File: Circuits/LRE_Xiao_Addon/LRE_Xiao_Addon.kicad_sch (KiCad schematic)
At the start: 13 parts, among them J1 Conn_01x06_Socket, J3 Conn_01x06_Socket, J4 Conn_01x02_Pin, Q1 S8050, Q2 S8050, Q3 S8050

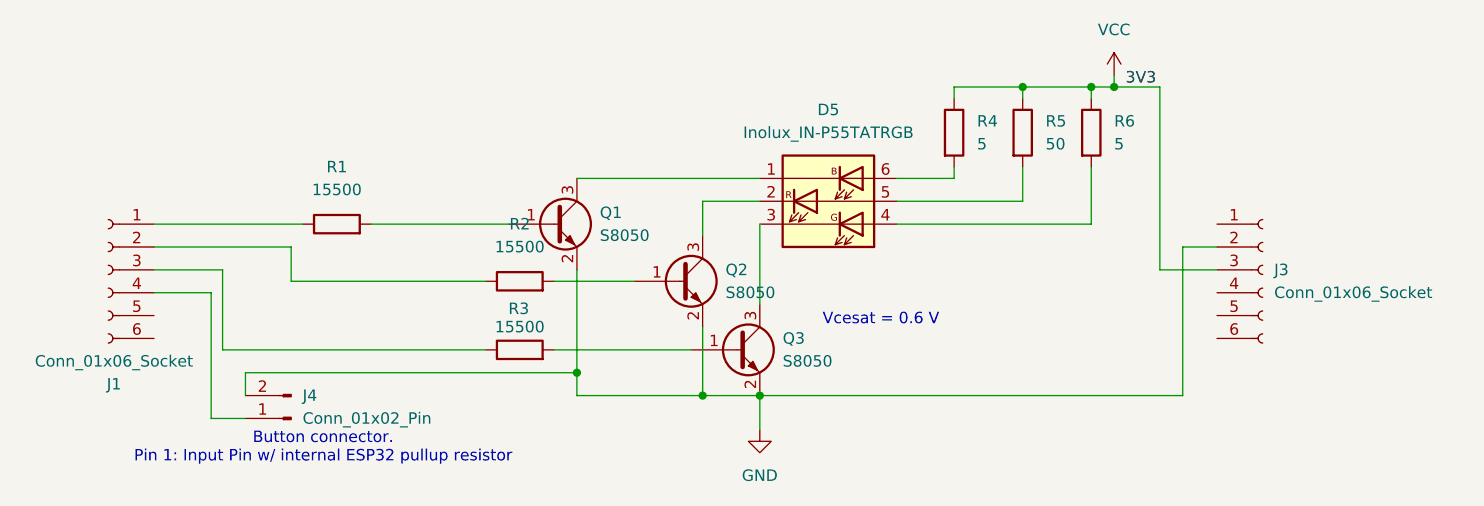
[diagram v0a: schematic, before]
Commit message: updated resistors
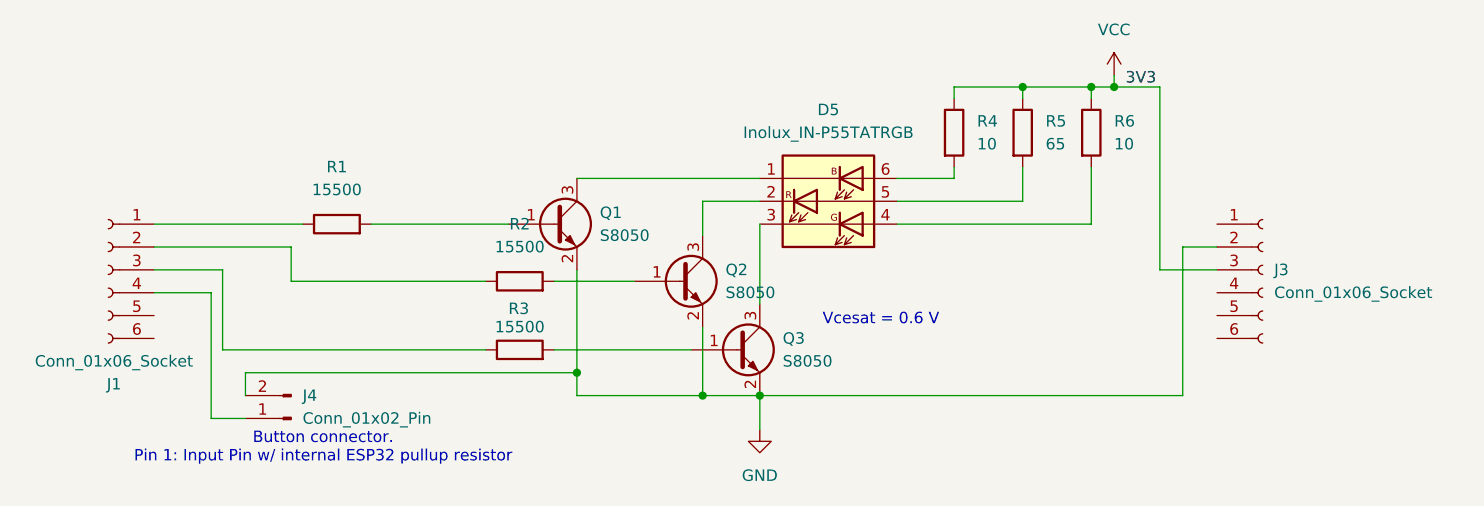
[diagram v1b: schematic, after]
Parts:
- R4, R6: value 5 -> 10
- R5: value 50 -> 65
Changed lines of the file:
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@@
 			)
 		)
-		(property "Value" "5"
+		(property "Value" "10"
 			(at 111.76 31.7499 0)
 			(effects
@@
 			)
 		)
-		(property "Value" "50"
+		(property "Value" "65"
 			(at 119.38 31.7499 0)
 			(effects
@@
 			)
 		)
-		(property "Value" "5"
+		(property "Value" "10"
 			(at 127 31.7499 0)
 			(effects

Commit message: USB Port accessible, updated color scheme
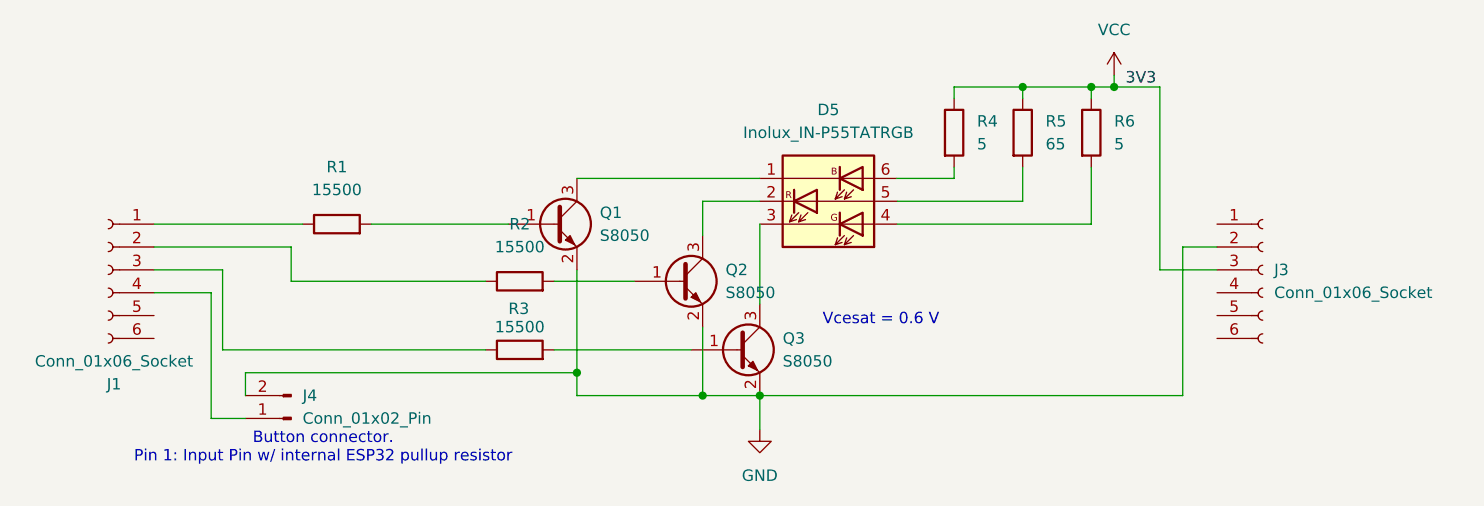
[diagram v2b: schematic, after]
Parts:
- R4, R6: value 10 -> 5
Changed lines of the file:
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@@
 			)
 		)
-		(property "Value" "10"
+		(property "Value" "5"
 			(at 111.76 31.7499 0)
 			(effects
@@
 			)
 		)
-		(property "Value" "10"
+		(property "Value" "5"
 			(at 127 31.7499 0)
 			(effects

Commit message: adjust resistors
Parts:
- R4, R6: value 5 -> 10,8
- R5: value 65 -> 60,8
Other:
- note added: "Vce = 0.084 V @ 20mA Ic (measured)"
- note removed: "Vcesat = 0.6 V"
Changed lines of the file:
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@@
 	(generator_version "9.0")
 	(paper "A4")
-	(text "Vcesat = 0.6 V"
-		(exclude_from_sim no)
-		(at 101.092 51.308 0)
+	(text "Vce = 0.084 V @ 20mA Ic (measured)"
+		(exclude_from_sim no)
+		(at 113.792 53.34 0)
 		(effects
 			(font
@@
 			)
 		)
-		(property "Datasheet" "https://mm.digikey.com/Volume0/opasdata/d220001/medias/docus/7158/5272_S8050.pdf"
+		(property "Datasheet" ""
 			(at 78.74 46.99 0)
 			(effects
@@
 		(dnp no)
 		(property "Reference" "R2"
-			(at 60.96 40.64 90)
+			(at 60.96 43.18 90)
 			(effects
 				(font
@@
 		)
 		(property "Value" "15500"
-			(at 60.96 43.18 90)
+			(at 60.96 44.958 90)
 			(effects
 				(font
@@
 		(on_board yes)
 		(dnp no)
-		(fields_autoplaced yes)
 		(property "Reference" "R4"
 			(at 111.76 29.2099 0)
@@
 			)
 		)
-		(property "Value" "5"
-			(at 111.76 31.7499 0)
+		(property "Value" "10,8"
+			(at 110.998 31.75 0)
 			(effects
 				(font
@@
 		(on_board yes)
 		(dnp no)
-		(fields_autoplaced yes)
 		(property "Reference" "R5"
 			(at 119.38 29.2099 0)
@@
 			)
 		)
-		(property "Value" "65"
-			(at 119.38 31.7499 0)
+		(property "Value" "60,8"
+			(at 118.364 31.75 0)
 			(effects
 				(font
@@
 			)
 		)
-		(property "Datasheet" "https://mm.digikey.com/Volume0/opasdata/d220001/medias/docus/7158/5272_S8050.pdf"
+		(property "Datasheet" ""
 			(at 85.09 54.61 0)
 			(effects
@@
 		(on_board yes)
 		(dnp no)
-		(fields_autoplaced yes)
 		(property "Reference" "R6"
 			(at 127 29.2099 0)
@@
 			)
 		)
-		(property "Value" "5"
-			(at 127 31.7499 0)
+		(property "Value" "10,8"
+			(at 127 31.75 0)
 			(effects
 				(font
@@
 		(on_board yes)
 		(dnp no)
-		(fields_autoplaced yes)
 		(property "Reference" "R1"
-			(at 40.64 34.29 90)
+			(at 40.64 36.83 90)
 			(do_not_autoplace yes)
 			(effects
@@
 		)
 		(property "Value" "15500"
-			(at 40.64 36.83 90)
+			(at 40.894 38.608 90)
 			(effects
 				(font
@@
 			)
 		)
-		(property "Datasheet" "https://mm.digikey.com/Volume0/opasdata/d220001/medias/docus/7158/5272_S8050.pdf"
+		(property "Datasheet" ""
 			(at 64.77 40.64 0)
 			(effects

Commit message: update hardware info
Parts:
- R4, R6: value 10,8 -> 11
- R5: value 60,8 -> 61
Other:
- note added: "Vce = 0.084 V @ 20mA Ic (measured) assuming Vce = 0,08V @ 20 mA for calculation"
- note removed: "Vce = 0.084 V @ 20mA Ic (measured)"
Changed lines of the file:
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@@
 	(generator_version "9.0")
 	(paper "A4")
-	(text "Vce = 0.084 V @ 20mA Ic (measured)"
-		(exclude_from_sim no)
-		(at 113.792 53.34 0)
+	(text "Vce = 0.084 V @ 20mA Ic (measured)\nassuming Vce = 0,08V @ 20 mA for calculation"
+		(exclude_from_sim no)
+		(at 113.538 49.53 0)
 		(effects
 			(font
@@
 			)
 		)
-		(property "Datasheet" ""
+		(property "Datasheet" "https://mm.digikey.com/Volume0/opasdata/d220001/medias/docus/7158/5272_S8050.pdf"
 			(at 78.74 46.99 0)
 			(effects
@@
 			)
 		)
-		(property "Value" "10,8"
+		(property "Value" "11"
 			(at 110.998 31.75 0)
 			(effects
@@
 			)
 		)
-		(property "Value" "60,8"
+		(property "Value" "61"
 			(at 118.364 31.75 0)
 			(effects
@@
 			)
 		)
-		(property "Datasheet" ""
+		(property "Datasheet" "https://mm.digikey.com/Volume0/opasdata/d220001/medias/docus/7158/5272_S8050.pdf"
 			(at 85.09 54.61 0)
 			(effects
@@
 			)
 		)
-		(property "Value" "10,8"
+		(property "Value" "11"
 			(at 127 31.75 0)
 			(effects
@@
 			)
 		)
-		(property "Datasheet" ""
+		(property "Datasheet" "https://mm.digikey.com/Volume0/opasdata/d220001/medias/docus/7158/5272_S8050.pdf"
 			(at 64.77 40.64 0)
 			(effects

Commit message: PCB v0.5
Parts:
- added J2: Conn_01x02_Socket, Connector_PinHeader_2.54mm:PinHeader_1x02_P2.54mm_Vertical, symbol Connector:Conn_01x02_Socket
- added R7, R8: 200k, Resistor_SMD:R_0805_2012Metric_Pad1.20x1.40mm_HandSolder, symbol Device:R
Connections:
- net at R2.1: now also J1.5 (Pin_5); no longer J1.2 (Pin_2)
- net at R3.1: now also J1.6 (Pin_6); no longer J1.3 (Pin_3)
- net at J4.1 (Pin_1): now also J3.4 (Pin_4); no longer J1.4 (Pin_4)
- net at R1.1: now also J1.4 (Pin_4); no longer J1.1 (Pin_1)
- new net: J2.1 (Pin_1), R8.2
- new net: J2.2 (Pin_2), R7.1, R8.1
- new net: J1.2 (Pin_2), R7.2
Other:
- moved on the sheet: J4, R1
